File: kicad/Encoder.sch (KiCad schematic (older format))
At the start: 4 parts, among them J10 ENC_Slave, J9 ENC_Host, U4 AS5048A

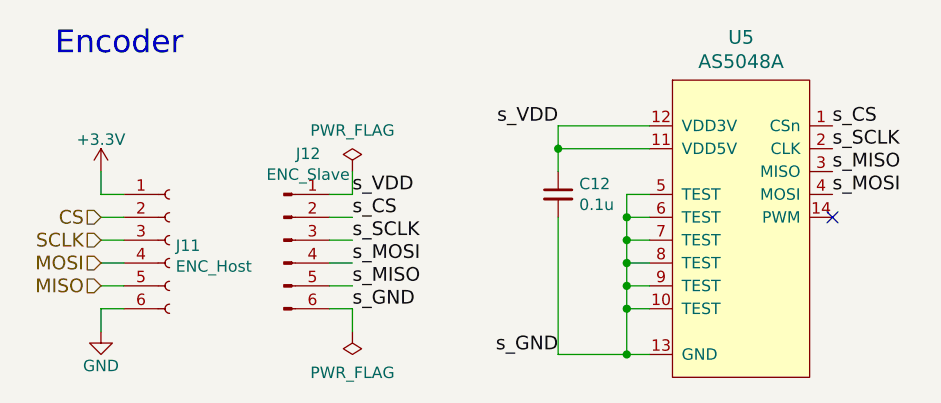
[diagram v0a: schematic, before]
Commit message: 部品を配置
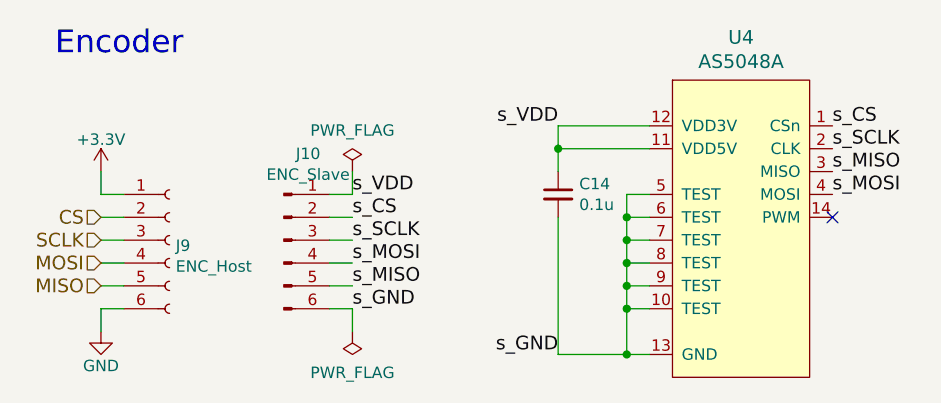
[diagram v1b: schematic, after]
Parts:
- renumbered C11 to C14
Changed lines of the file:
@@
 $EndDescr
 $Comp
-L power:GND #PWR050
+L power:GND #PWR052
 U 1 1 589E94E9
 P 4100 3600
-AR Path="/592ADBF2/589E94E9" Ref="#PWR050"  Part="1"
-AR Path="/59347BCD/589E94E9" Ref="#PWR052"  Part="1"
-F 0 "#PWR052" H 4100 3350 50  0001 C CNN
+AR Path="/592ADBF2/589E94E9" Ref="#PWR052"  Part="1"
+AR Path="/59347BCD/589E94E9" Ref="#PWR054"  Part="1"
+F 0 "#PWR054" H 4100 3350 50  0001 C CNN
 F 1 "GND" H 4100 3450 50  0000 C CNN
 F 2 "" H 4100 3600 50  0000 C CNN
@@
 $EndComp
 $Comp
-L power:+3.3V #PWR049
+L power:+3.3V #PWR051
 U 1 1 589CCACF
 P 4100 2900
-AR Path="/592ADBF2/589CCACF" Ref="#PWR049"  Part="1"
-AR Path="/59347BCD/589CCACF" Ref="#PWR051"  Part="1"
-F 0 "#PWR051" H 4100 2750 50  0001 C CNN
+AR Path="/592ADBF2/589CCACF" Ref="#PWR051"  Part="1"
+AR Path="/59347BCD/589CCACF" Ref="#PWR053"  Part="1"
+F 0 "#PWR053" H 4100 2750 50  0001 C CNN
 F 1 "+3.3V" H 4100 3040 50  0000 C CNN
 F 2 "" H 4100 2900 50  0000 C CNN
@@
 AR Path="/592ADBF2/5B6F84B0" Ref="J9"  Part="1"
 AR Path="/59347BCD/5B6F84B0" Ref="J11"  Part="1"
-F 0 "J11" H 4427 3176 50  0000 L CNN
+F 0 "J9" H 4427 3176 50  0000 L CNN
 F 1 "ENC_Host" H 4427 3085 50  0000 L CNN
 F 2 "mouse:STAND_HOST_06" H 4400 3200 50  0001 C CNN
@@
 AR Path="/592ADBF2/5B6F8513" Ref="J10"  Part="1"
 AR Path="/59347BCD/5B6F8513" Ref="J12"  Part="1"
-F 0 "J12" H 5006 3578 50  0000 C CNN
+F 0 "J10" H 5006 3578 50  0000 C CNN
 F 1 "ENC_Slave" H 5006 3487 50  0000 C CNN
 F 2 "mouse:STAND_SLAVE_06" H 4900 3200 50  0001 C CNN
@@
 AR Path="/592ADBF2/5C2A3915" Ref="U4"  Part="1"
 AR Path="/59347BCD/5C2A3915" Ref="U5"  Part="1"
-F 0 "U5" H 6900 3687 60  0000 C CNN
+F 0 "U4" H 6900 3687 60  0000 C CNN
 F 1 "AS5048A" H 6900 3581 60  0000 C CNN
 F 2 "mouse:TSSOP-14_4.4x5mm_Pitch0.65mm" H 6900 3400 60  0001 C CNN
@@
 s_VDD
 $Comp
-L Device:C_Small C11
+L Device:C_Small C14
 U 1 1 5C2A3C19
 P 6100 3000
-AR Path="/592ADBF2/5C2A3C19" Ref="C11"  Part="1"
-AR Path="/59347BCD/5C2A3C19" Ref="C12"  Part="1"
-F 0 "C12" H 6192 3046 50  0000 L CNN
+AR Path="/592ADBF2/5C2A3C19" Ref="C14"  Part="1"
+AR Path="/59347BCD/5C2A3C19" Ref="C15"  Part="1"
+F 0 "C14" H 6192 3046 50  0000 L CNN
 F 1 "0.1u" H 6192 2955 50  0000 L CNN
 F 2 "Capacitor_SMD:C_0201_0603Metric" H 6100 3000 50  0001 C CNN

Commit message: フットプリントを改良
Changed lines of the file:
@@
 AR Path="/592ADBF2/5B6F84B0" Ref="J9"  Part="1"
 AR Path="/59347BCD/5B6F84B0" Ref="J11"  Part="1"
-F 0 "J9" H 4427 3176 50  0000 L CNN
+F 0 "J11" H 4427 3176 50  0000 L CNN
 F 1 "ENC_Host" H 4427 3085 50  0000 L CNN
 F 2 "mouse:STAND_HOST_06" H 4400 3200 50  0001 C CNN
@@
 AR Path="/592ADBF2/5B6F8513" Ref="J10"  Part="1"
 AR Path="/59347BCD/5B6F8513" Ref="J12"  Part="1"
-F 0 "J10" H 5006 3578 50  0000 C CNN
+F 0 "J12" H 5006 3578 50  0000 C CNN
 F 1 "ENC_Slave" H 5006 3487 50  0000 C CNN
 F 2 "mouse:STAND_SLAVE_06" H 4900 3200 50  0001 C CNN
@@
 AR Path="/592ADBF2/5C2A3915" Ref="U4"  Part="1"
 AR Path="/59347BCD/5C2A3915" Ref="U5"  Part="1"
-F 0 "U4" H 6900 3687 60  0000 C CNN
+F 0 "U5" H 6900 3687 60  0000 C CNN
 F 1 "AS5048A" H 6900 3581 60  0000 C CNN
 F 2 "mouse:TSSOP-14_4.4x5mm_Pitch0.65mm" H 6900 3400 60  0001 C CNN
@@
 AR Path="/592ADBF2/5C2A3C19" Ref="C14"  Part="1"
 AR Path="/59347BCD/5C2A3C19" Ref="C15"  Part="1"
-F 0 "C14" H 6192 3046 50  0000 L CNN
+F 0 "C15" H 6192 3046 50  0000 L CNN
 F 1 "0.1u" H 6192 2955 50  0000 L CNN
 F 2 "Capacitor_SMD:C_0201_0603Metric" H 6100 3000 50  0001 C CNN
